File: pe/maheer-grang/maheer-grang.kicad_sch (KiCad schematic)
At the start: 12 parts, among them U1 AP62300TWU

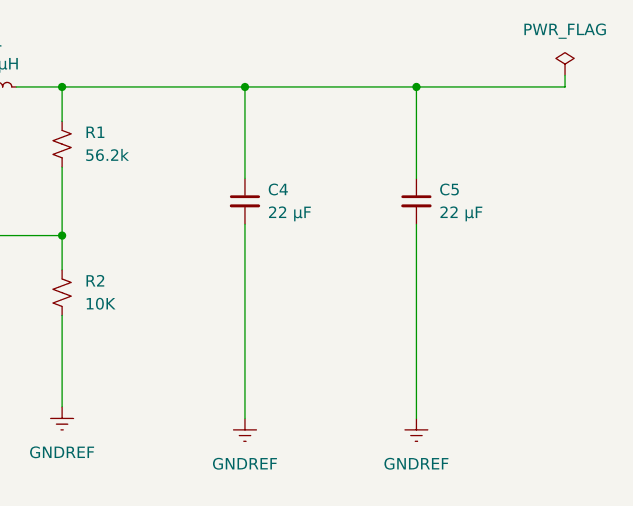
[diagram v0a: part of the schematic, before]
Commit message: updated the buck schematic (added digikey PN/links and 1 more output cap)
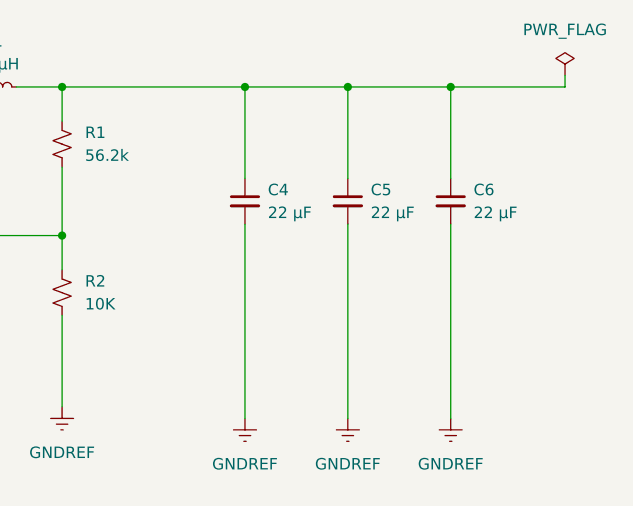
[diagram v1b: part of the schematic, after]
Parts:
- added C6: 22 µF, Capacitor_SMD:C_0603_1608Metric_Pad1.08x0.95mm_HandSolder, symbol Device:C_Small
- U1: Digikey Part Number (none) -> 31-AP62300TWU-7CT-ND; Digikey URL (none) -> https://www.digikey.com/en/products/detail/diodes-incorpora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; Manufacturer (none) -> Diodes Incorporated; Manufacturer Part Number (none) -> AP62300TWU-7
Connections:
- net GNDREF: now also C6.2
- net at C4.1, C5.1, L1.2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: now also C6.1
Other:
- moved on the sheet: C5
